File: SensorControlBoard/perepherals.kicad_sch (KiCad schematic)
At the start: 36 parts, among them J1 Micro_SD_Card, U10 ASMB-TTF0-0A20B, U11 ASMB-TTF0-0A20B, U12 AT24CS04-XHM, U13 OPT3002DNPR, U5 LP5018RSMR, U6 ASMB-TTF0-0A20B, U7 ASMB-TTF0-0A20B, U8 ASMB-TTF0-0A20B, U9 ASMB-TTF0-0A20B

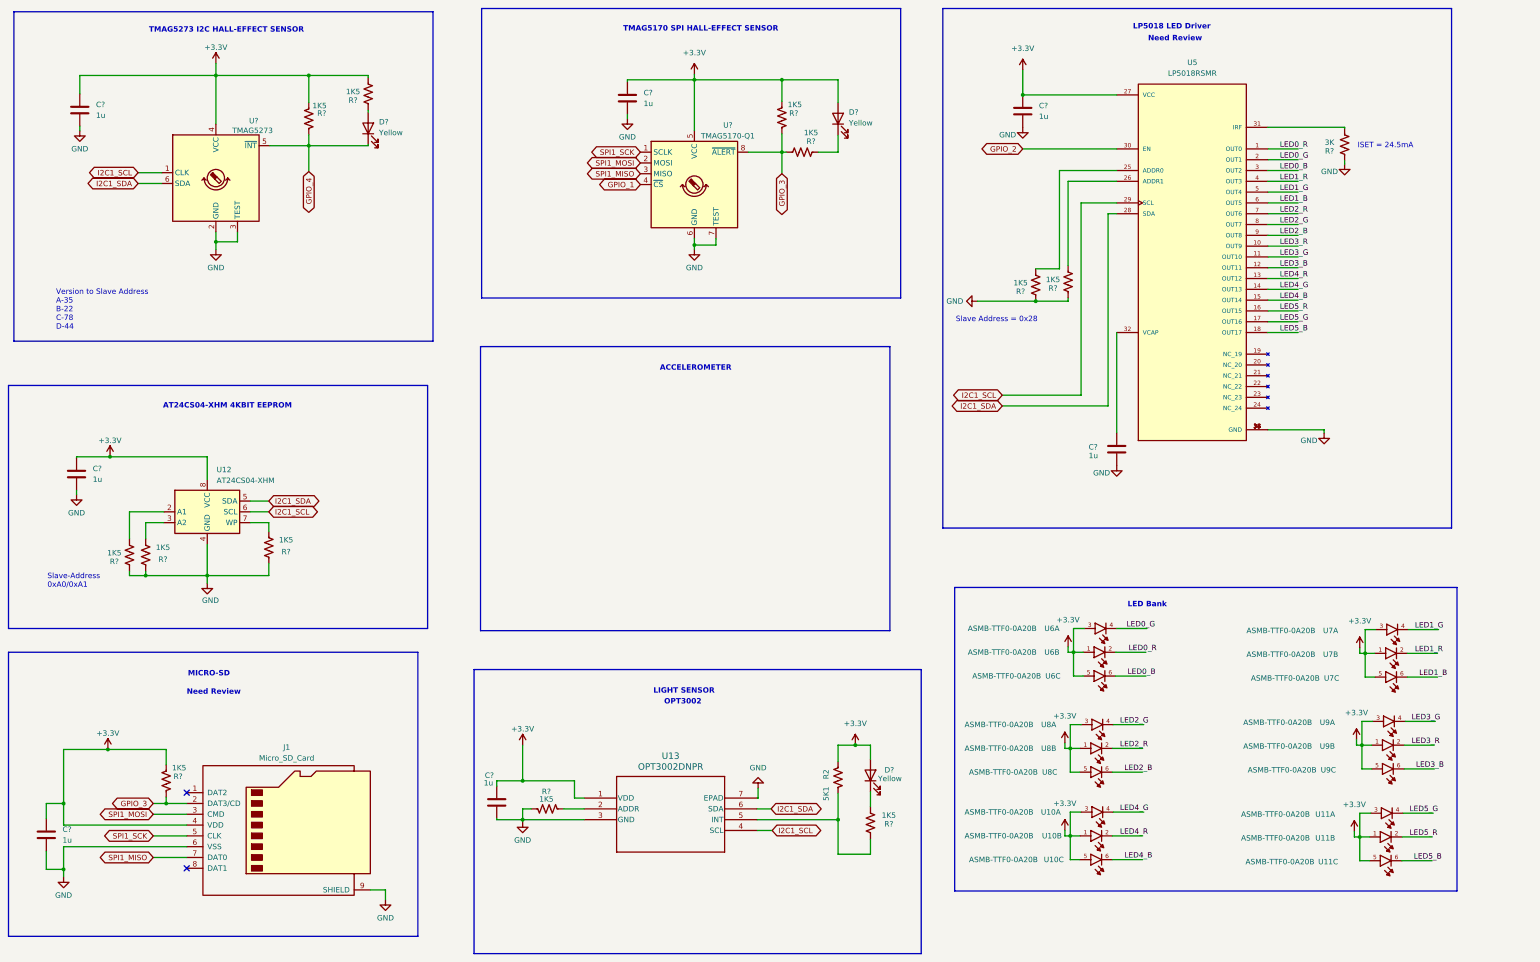
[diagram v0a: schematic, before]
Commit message: Implemented ICM-42670-P 6 axis gyroscope/accelerometer
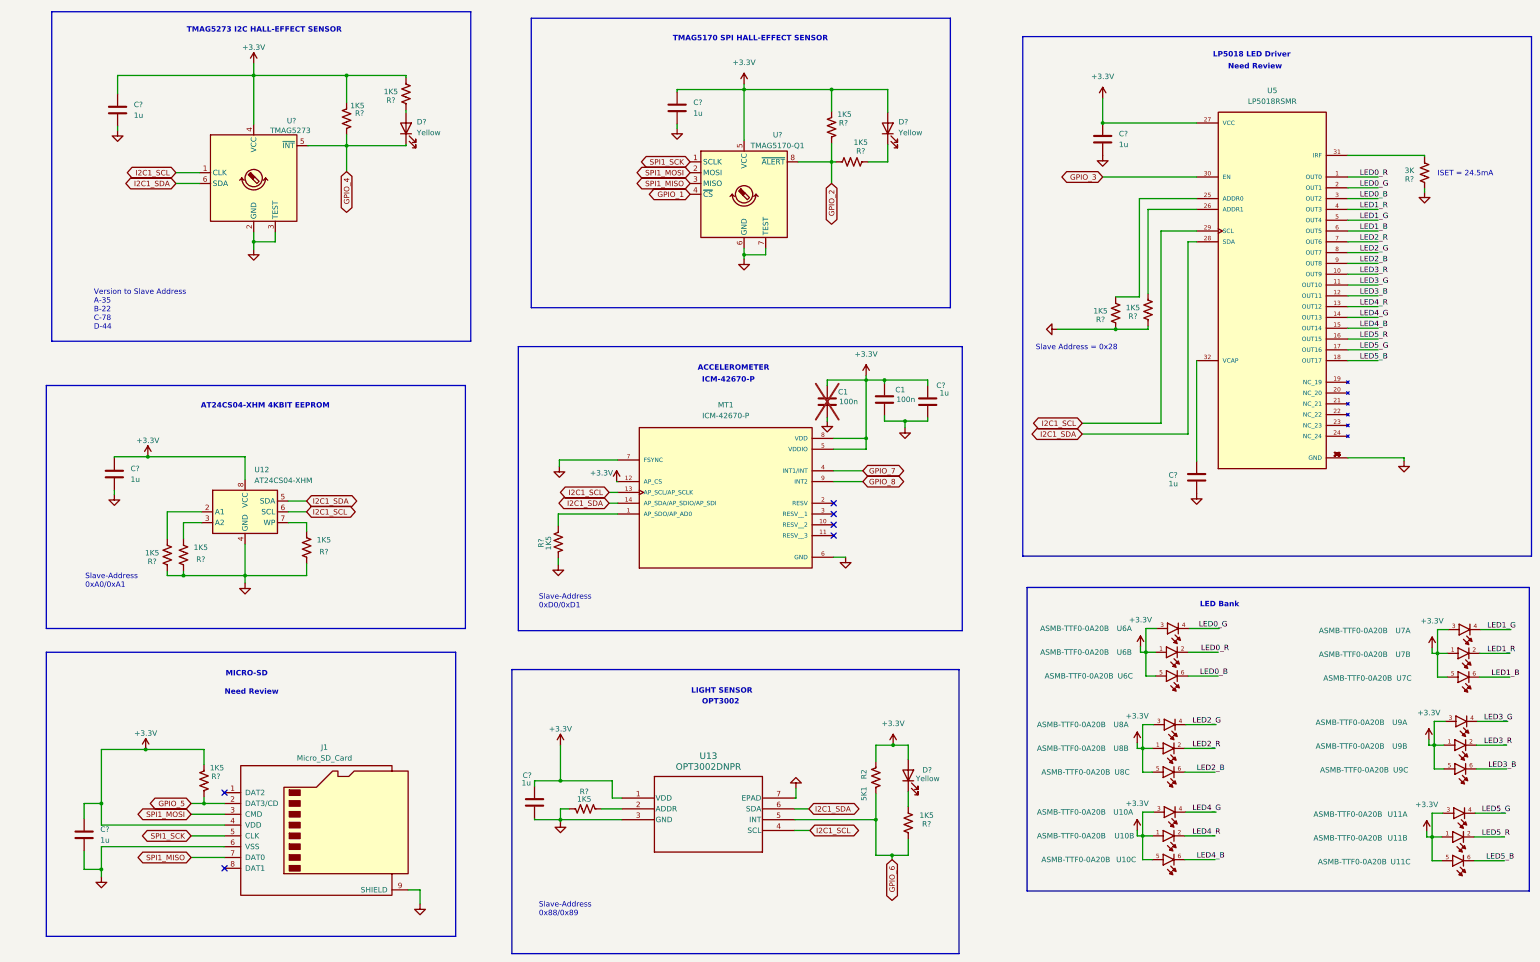
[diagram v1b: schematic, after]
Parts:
- added C1 (x2): 100n, Resistor_SMD:R_0805_2012Metric, symbol Device:C
- added C?: 1u, Resistor_SMD:R_0805_2012Metric, symbol Device:C
- added MT1: ICM-42670-P, ICM-42670-P:XDCR_ICM-42670-P, symbol ICM-42670-P:ICM-42670-P
- added R?: 1K5, Resistor_SMD:R_0805_2012Metric, symbol Device:R_US
- C? (x7), D? (x3), J1, R2, R? (x13): footprint (none) -> Resistor_SMD:R_0805_2012Metric
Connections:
- net +3.3V: now also C1.1, C1.1, C?.1, MT1.12 (AP_CS), MT1.5 (VDDIO), MT1.8 (VDD)
- net GND: now also C1.2, C1.2, C?.2, MT1.6 (GND), MT1.7 (FSYNC), R?.1
- net GPIO_2: now also R?.2, R?.2, U?.8 (~{ALERT}); no longer U5.30 (EN)
- net GPIO_3: now also U5.30 (EN); no longer J1.2 (DAT3/CD), R?.2, R?.2, R?.2, U?.8 (~{ALERT})
- net I2C1_SCL: now also MT1.13 (AP_SCL/AP_SCLK)
- net I2C1_SDA: now also MT1.14 (AP_SDA/AP_SDIO/AP_SDI)
- net GPIO_6: now reaches R2.1, R?.2, U13.5 (INT)
- new net: MT1.1 (AP_SDO/AP_AD0), R?.2
- new net GPIO_5: J1.2 (DAT3/CD), R?.2
- new net GPIO_7: MT1.4 (INT1/INT)
- new net GPIO_8: MT1.9 (INT2)
- no-connect marks 2 -> 6
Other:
- note added: "ICM-42670-P"
- note added: "Slave-Address 0x88/0x89"
- note added: "Slave-Address 0xD0/0xD1"
- moved on the sheet: C?, D?, J1, R2, R?, U10A, U10B, U10C, U11A, U11B, U11C, U12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

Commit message: Added more schematic documentation to prepare for hardware layout
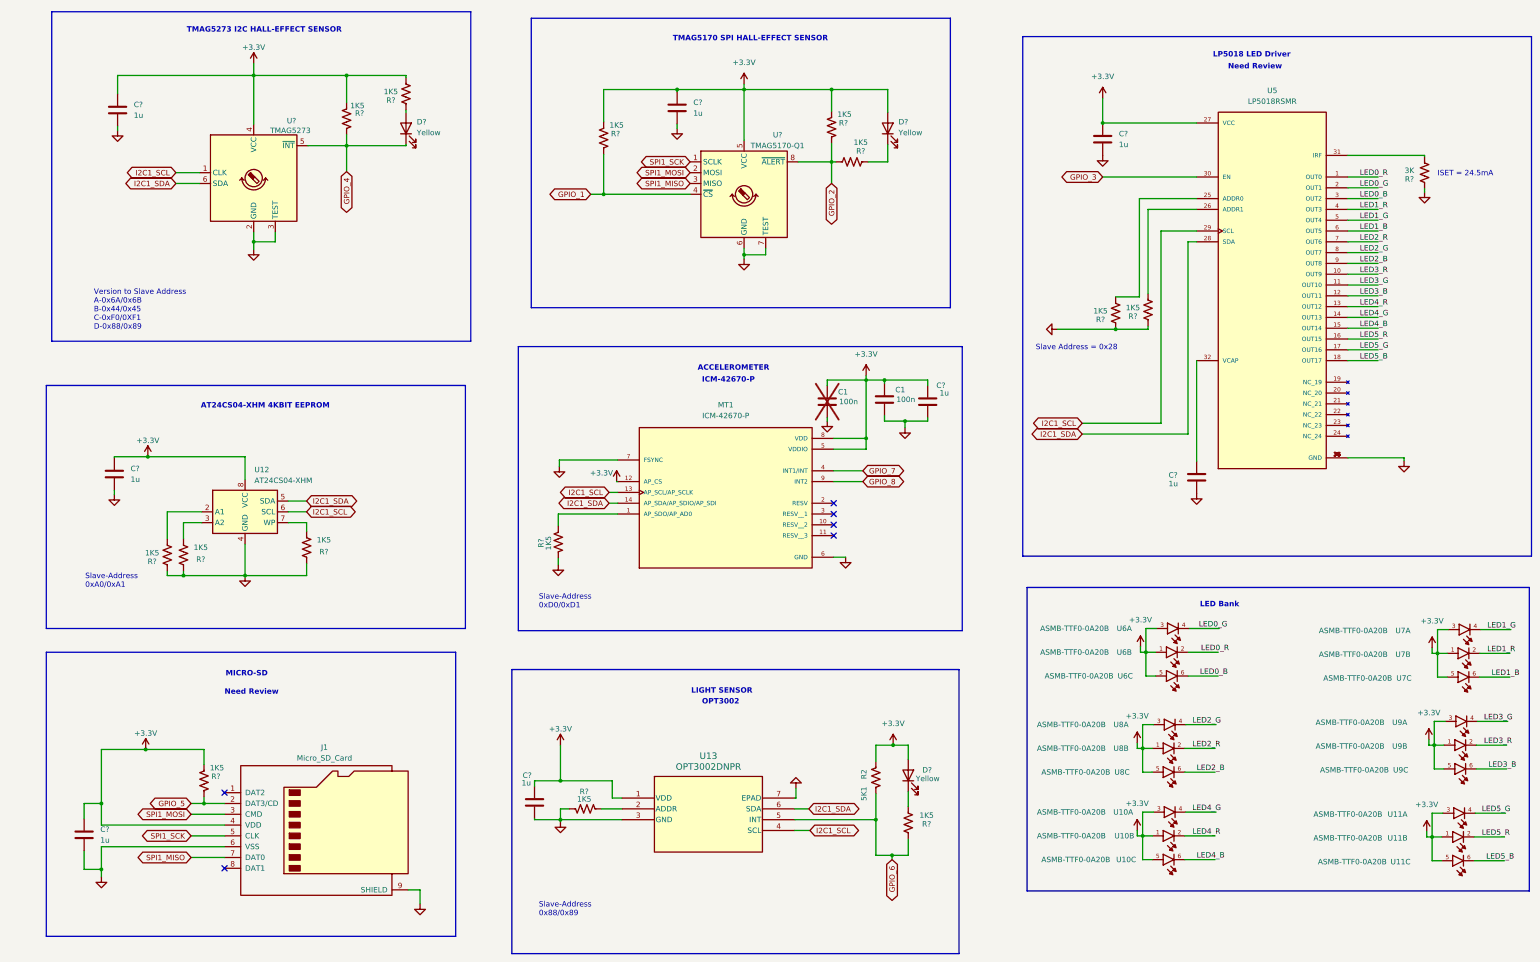
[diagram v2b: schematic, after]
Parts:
- added R?: 1K5, Resistor_SMD:R_0805_2012Metric, symbol Device:R_US
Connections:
- net +3.3V: now also R?.1
- net GPIO_1: now also R?.2
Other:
- note added: "Version to Slave Address A-0x6A/0x6B B-0x44/0x45 C-0xF0/0XF1 D-0x88/0x89"
- note removed: "Version to Slave Address A-35 B-22 C-78 D-44"
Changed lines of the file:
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@@
   (junction (at 80.01 158.242) (diameter 0) (color 0 0 0 0)
   )
+  (junction (at 164.338 68.58) (diameter 0) (color 0 0 0 0)
+  )
   (junction (at 359.664 198.12) (diameter 0) (color 0 0 0 0)
   )
@@
   (junction (at 154.178 215.646) (diameter 0) (color 0 0 0 0)
   )
+  (junction (at 226.06 125.984) (diameter 0) (color 0 0 0 0)
+  )
   (junction (at 226.06 112.268) (diameter 0) (color 0 0 0 0)
   )
-  (junction (at 226.06 125.984) (diameter 0) (color 0 0 0 0)
+  (junction (at 181.61 43.942) (diameter 0) (color 0 0 0 0)
   )
   (junction (at 217.932 43.942) (diameter 0) (color 0 0 0 0)
@@
     (stroke (width 0) (type default))
   )
-  (wire (pts (xy 216.916 112.268) (xy 226.06 112.268))
+  (wire (pts (xy 161.29 68.58) (xy 164.338 68.58))
     (stroke (width 0) (type default))
   )
@@
     (stroke (width 0) (type default))
   )
+  (wire (pts (xy 164.338 51.562) (xy 164.338 43.942))
+    (stroke (width 0) (type default))
+  )
   (wire (pts (xy 339.344 89.916) (xy 346.456 89.916))
     (stroke (width 0) (type default))
@@
     (stroke (width 0) (type default))
   )
-  (wire (pts (xy 168.656 213.106) (xy 163.83 213.106))
-    (stroke (width 0) (type default))
-  )
   (wire (pts (xy 148.082 206.502) (xy 154.178 206.502))
     (stroke (width 0) (type default))
@@
     (stroke (width 0) (type default))
   )
-  (wire (pts (xy 281.686 64.516) (xy 303.784 64.516))
-    (stroke (width 0) (type default))
-  )
   (wire (pts (xy 197.358 82.804) (xy 202.438 82.804))
     (stroke (width 0) (type default))
@@
     (stroke (width 0) (type default))
   )
+  (wire (pts (xy 164.338 68.58) (xy 184.658 68.58))
+    (stroke (width 0) (type default))
+  )
   (wire (pts (xy 168.656 215.646) (xy 154.178 215.646))
     (stroke (width 0) (type default))
@@
     (stroke (width 0) (type default))
   )
-  (wire (pts (xy 80.01 158.242) (xy 80.01 160.02))
-    (stroke (width 0) (type default))
-  )
   (wire (pts (xy 339.344 69.596) (xy 346.456 69.596))
     (stroke (width 0) (type default))
@@
     (stroke (width 0) (type default))
   )
-  (wire (pts (xy 94.488 158.242) (xy 80.01 158.242))
-    (stroke (width 0) (type default))
-  )
   (wire (pts (xy 61.722 143.256) (xy 61.722 149.606))
     (stroke (width 0) (type default))
@@
     (stroke (width 0) (type default))
   )
+  (wire (pts (xy 164.338 68.58) (xy 164.338 59.182))
+    (stroke (width 0) (type default))
+  )
   (wire (pts (xy 167.386 136.144) (xy 167.64 136.144))
     (stroke (width 0) (type default))
@@
     (stroke (width 0) (type default))
   )
+  (wire (pts (xy 163.83 213.106) (xy 168.656 213.106))
+    (stroke (width 0) (type default))
+  )
   (wire (pts (xy 218.44 153.924) (xy 221.234 153.924))
     (stroke (width 0) (type default))
@@
     (stroke (width 0) (type default))
   )
+  (wire (pts (xy 80.01 158.242) (xy 94.488 158.242))
+    (stroke (width 0) (type default))
+  )
   (wire (pts (xy 360.426 182.118) (xy 360.426 176.53))
     (stroke (width 0) (type default))
@@
     (stroke (width 0) (type default))
   )
+  (wire (pts (xy 226.06 112.268) (xy 230.378 112.268))
+    (stroke (width 0) (type default))
+  )
   (wire (pts (xy 370.332 176.53) (xy 377.444 176.53))
     (stroke (width 0) (type default))
@@
     (stroke (width 0) (type default))
   )
-  (wire (pts (xy 230.378 112.268) (xy 226.06 112.268))
+  (wire (pts (xy 216.916 112.268) (xy 226.06 112.268))
     (stroke (width 0) (type default))
   )
@@
     (stroke (width 0) (type default))
   )
+  (wire (pts (xy 281.686 64.516) (xy 303.784 64.516))
+    (stroke (width 0) (type default))
+  )
   (wire (pts (xy 301.244 213.868) (xy 308.356 213.868))
     (stroke (width 0) (type default))
@@
     (stroke (width 0) (type default))
   )
+  (wire (pts (xy 164.338 43.942) (xy 181.61 43.942))
+    (stroke (width 0) (type default))
+  )
   (wire (pts (xy 69.85 145.796) (xy 65.532 145.796))
     (stroke (width 0) (type default))
@@
     (effects (font (size 1.27 1.27) (thickness 0.254) bold) (justify left bottom))
   )
-  (text "Version to Slave Address\nA-35\nB-22\nC-78\nD-44" (at 44.45 100.584 0)
+  (text "Version to Slave Address\nA-0x6A/0x6B\nB-0x44/0x45\nC-0xF0/0XF1\nD-0x88/0x89"
+    (at 44.45 100.584 0)
     (effects (font (size 1.27 1.27)) (justify left bottom))
   )
@@
     )
   )
-  (global_label "GPIO_1" (shape bidirectional) (at 184.658 68.58 180) (fields_autoplaced)
+  (global_label "GPIO_1" (shape bidirectional) (at 161.29 68.58 180) (fields_autoplaced)
     (effects (font (size 1.27 1.27)) (justify right))
-    (property "Intersheetrefs" "${INTERSHEET_REFS}" (at 173.9091 68.58 0)
+    (property "Intersheetrefs" "${INTERSHEET_REFS}" (at 150.5411 68.58 0)
       (effects (font (size 1.27 1.27)) (justify right) hide)
     )
@@
     )
   )
-  (symbol (lib_id "power:GND") (at 80.01 160.02 0) (unit 1)
-    (in_bom yes) (on_board yes) (dnp no)
-    (property "Reference" "#PWR044" (at 80.01 166.37 0)
-      (effects (font (size 1.27 1.27)) hide)
-    )
-    (property "Value" "GND" (at 80.772 164.084 0)
-      (effects (font (size 1.27 1.27)) hide)
-    )
-    (property "Footprint" "" (at 80.01 160.02 0)
-      (effects (font (size 1.27 1.27)) hide)
-    )
-    (property "Datasheet" "" (at 80.01 160.02 0)
-      (effects (font (size 1.27 1.27)) hide)
-    )
-    (pin "1")
-    (instances
-      (project "SensorControlBoard"
-        (path "/8c0c4014-aa51-4bf6-8434-aa4d122163d4/08ebbf42-81e7-4a5c-bbac-f4d91ee3da15"
-          (reference "#PWR044") (unit 1)
-        )
-      )
-      (project "untitled"
-        (path "/b4f2be72-1726-4a01-8474-da71fc549efc"
-          (reference "#PWR027") (unit 1)
-        )
-      )
-    )
-  )
   (symbol (lib_id "power:+3.3V") (at 56.642 199.136 0) (unit 1)
     (in_bom yes) (on_board yes) (dnp no)
@@
     )
   )
+  (symbol (lib_id "Device:R_US") (at 164.338 55.372 0) (mirror y) (unit 1)
+    (in_bom yes) (on_board yes) (dnp no)
+    (property "Reference" "R?" (at 167.132 54.356 0)
+      (effects (font (size 1.27 1.27)))
+    )
+    (property "Value" "1K5" (at 167.386 52.324 0)
+      (effects (font (size 1.27 1.27)))
+    )
+    (property "Footprint" "Resistor_SMD:R_0805_2012Metric" (at 163.322 55.626 90)
+      (effects (font (size 1.27 1.27)) hide)
+    )
+    (property "Datasheet" "~" (at 164.338 55.372 0)
+      (effects (font (size 1.27 1.27)) hide)
+    )
+    (pin "1")
+    (pin "2")
+    (instances
+      (project "SensorControlBoard"
+        (path "/8c0c4014-aa51-4bf6-8434-aa4d122163d4"
+          (reference "R?") (unit 1)
+        )
+        (path "/8c0c4014-aa51-4bf6-8434-aa4d122163d4/1219a1e8-5b4c-4ffc-965f-b8113c415640"
+          (reference "R1") (unit 1)
+        )
+        (path "/8c0c4014-aa51-4bf6-8434-aa4d122163d4/08ebbf42-81e7-4a5c-bbac-f4d91ee3da15"
+          (reference "R24") (unit 1)
+        )
+      )
+      (project "untitled"
+        (path "/b4f2be72-1726-4a01-8474-da71fc549efc"
+          (reference "R2") (unit 1)
+        )
+      )
+    )
+  )
   (symbol (lib_id "power:GND") (at 352.552 131.318 0) (unit 1)
     (in_bom yes) (on_board yes) (dnp no)
@@
         )
       )
+    )
+  )
+  (symbol (lib_id "power:GND") (at 80.01 158.242 0) (unit 1)
+    (in_bom yes) (on_board yes) (dnp no) (fields_autoplaced)
+    (property "Reference" "#PWR051" (at 80.01 164.592 0)
+      (effects (font (size 1.27 1.27)) hide)
+    )
+    (property "Value" "GND" (at 80.01 162.56 0)
+      (effects (font (size 1.27 1.27)) hide)
+    )
+    (property "Footprint" "" (at 80.01 158.242 0)
+      (effects (font (size 1.27 1.27)) hide)
+    )
+    (property "Datasheet" "" (at 80.01 158.242 0)
+      (effects (font (size 1.27 1.27)) hide)
+    )
+    (pin "1")
+    (instances
+      (project "SensorControlBoard"
+        (path "/8c0c4014-aa51-4bf6-8434-aa4d122163d4/08ebbf42-81e7-4a5c-bbac-f4d91ee3da15"
+          (reference "#PWR051") (unit 1)
+        )
+      )

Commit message: Initial placement done
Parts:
- C1: footprint Resistor_SMD:R_0805_2012Metric -> Capacitor_SMD:C_0603_1608Metric_Pad1.08x0.95mm_HandSolder; MP (none) -> C0805C104K5RAC7210
- C? (x8): footprint Resistor_SMD:R_0805_2012Metric -> Capacitor_SMD:C_0603_1608Metric_Pad1.08x0.95mm_HandSolder; MP (none) -> C0805C105Z4VAC7800
- D? (x3): footprint Resistor_SMD:R_0805_2012Metric -> LED_SMD:LED_0603_1608Metric_Pad1.05x0.95mm_HandSolder; MP (none) -> 150060YS75000
- J1: footprint Resistor_SMD:R_0805_2012Metric -> Connector_Card:microSD_HC_Hirose_DM3D-SF; MP (none) -> 2508051217Y6
- R2, R? (x15): footprint Resistor_SMD:R_0805_2012Metric -> Resistor_SMD:R_0603_1608Metric_Pad0.98x0.95mm_HandSolder
- U13: footprint DNP6_TEX -> ASMB-MTB1-0A3A2:DNP6_TEX
- U?: value TMAG5273 -> TMAG5273B1QDBVR
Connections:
- net AT24CS04-XHM_WP: now reaches R?.2, U12.7 (WP)
- net AT24CS04-XHM_A1: now reaches R?.2, U12.2 (A1)
- net AT24CS04-XHM_A2: now reaches R?.2, U12.3 (A2)
- net 5273_INT_IND_A: now reaches D?.2 (A), R?.1
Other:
- moved on the sheet: R?
